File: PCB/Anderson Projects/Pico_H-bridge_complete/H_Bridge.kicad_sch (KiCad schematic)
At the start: 36 parts, among them Q1 AO3400A, Q2 AO3400A, Q3 DMP3130LQ-7, Q4 DMP3130LQ-7, Q5 MMBT3904, Q6 MMBT3904, U10 SN74LVC1G14DBV, U12 SN74LVC1G32, U13 SN74LVC1G32, U2 74LVC1G08GV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

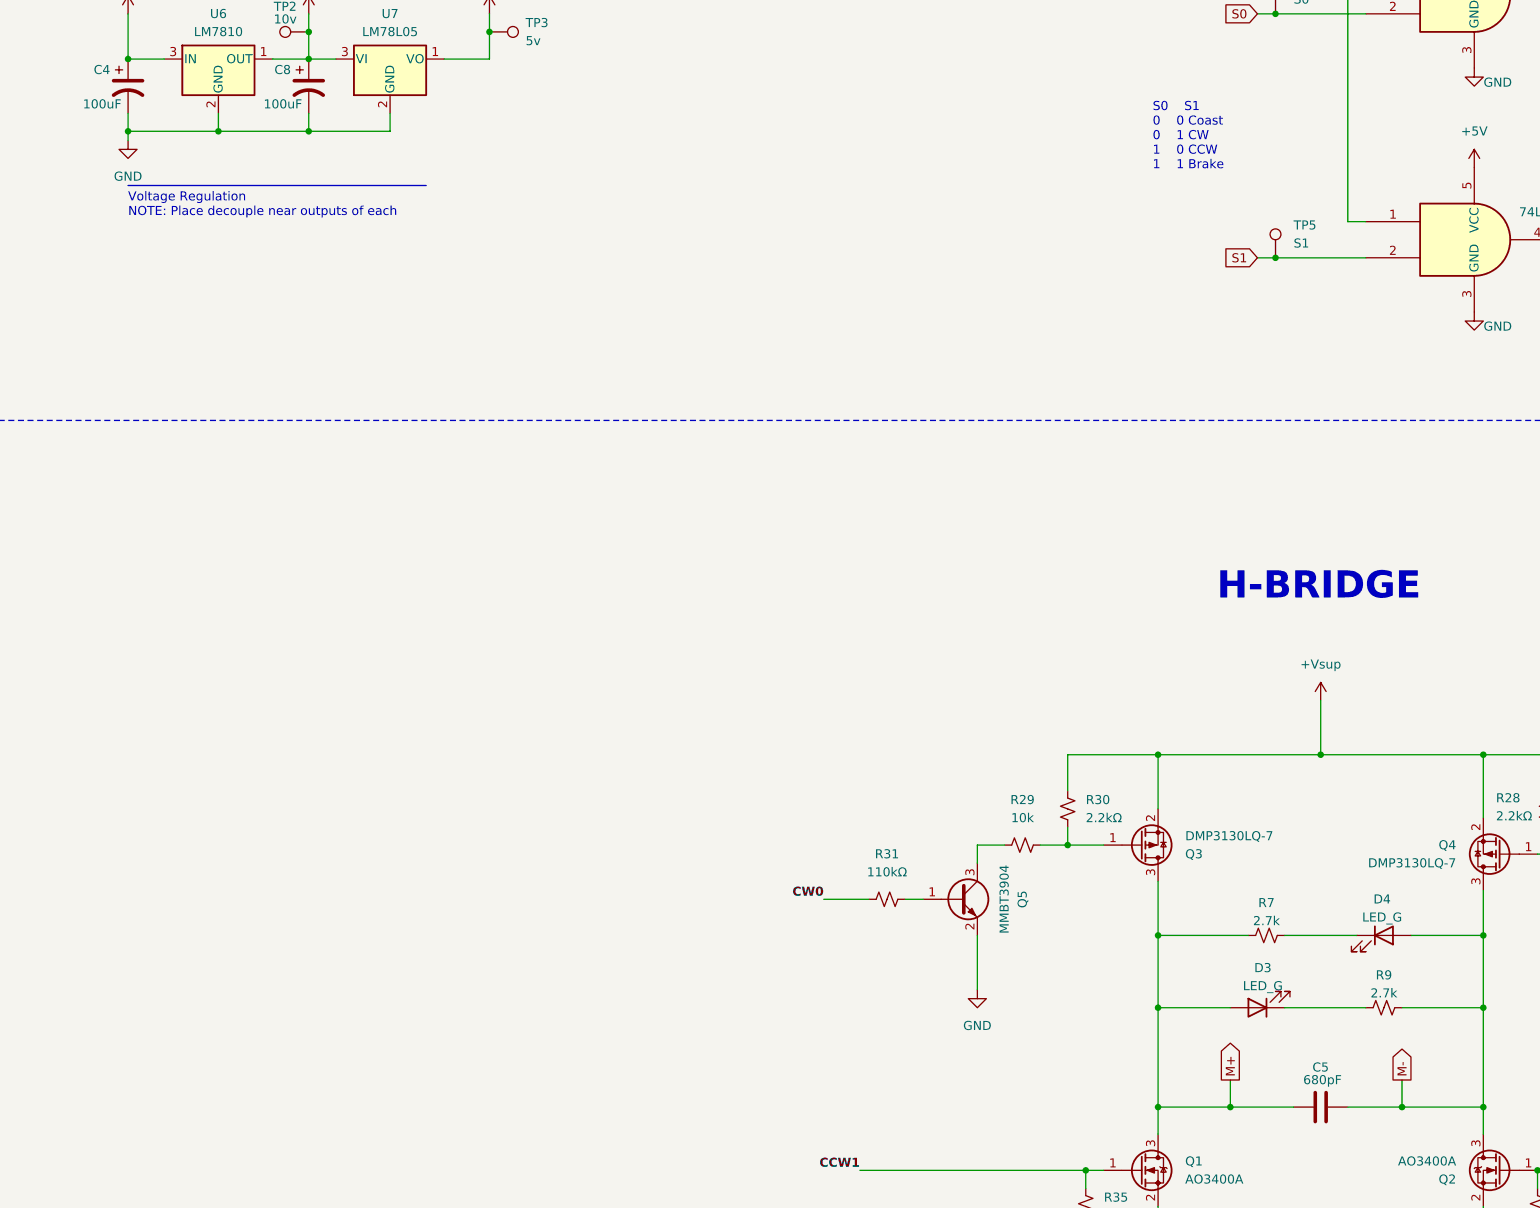
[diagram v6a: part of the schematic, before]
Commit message: Final Board version prior to testing motor with pulleys. This version would not turn the motor when connected to a generator. The Vgs values for Mosfets needed increased to 10v. Other improvements to make include removing braking functionality to simplify control to Fwd/Rev vice S0/S1.
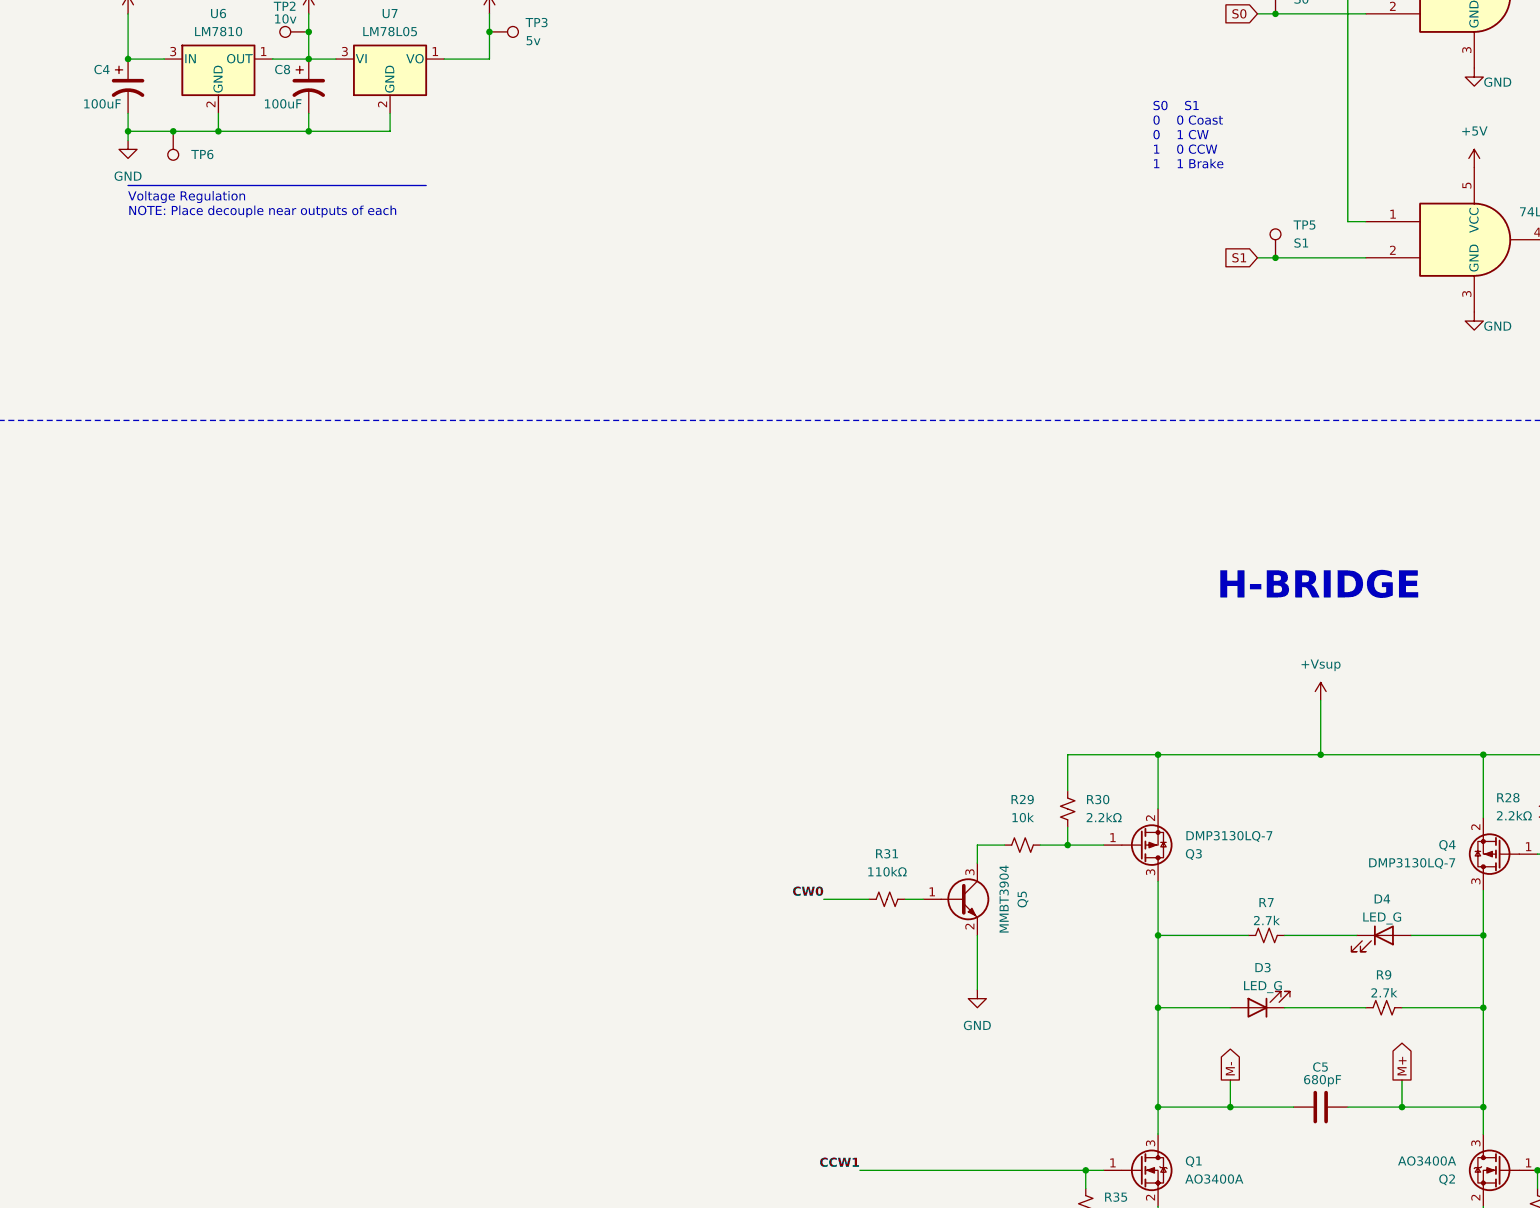
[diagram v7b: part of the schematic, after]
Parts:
- added TP6: GND, TestPoint:TestPoint_Loop_D2.60mm_Drill1.4mm_Beaded, symbol Connector:TestPoint
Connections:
- net GND: now also TP6.1
- net M+: now also C5.2, D4.2 (A), Q2.3 (D), Q4.3 (D), R9.1; no longer C5.1, D3.2 (A), Q1.3 (D), Q3.3 (D), R7.2
- net M-: now also C5.1, D3.2 (A), Q1.3 (D), Q3.3 (D), R7.2; no longer C5.2, D4.2 (A), Q2.3 (D), Q4.3 (D), R9.1
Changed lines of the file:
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@@
 	)
 	(junction
+		(at 50.8 87.63)
+		(diameter 0)
+		(color 0 0 0 0)
+	)
+	(junction
 		(at 176.53 187.96)
 		(diameter 0)
@@
 	(wire
 		(pts
+			(xy 50.8 87.63) (xy 57.15 87.63)
+		)
+		(stroke
+			(width 0)
+			(type default)
+		)
+	)
+	(wire
+		(pts
 			(xy 260.35 111.76) (xy 288.29 111.76)
 		)
@@
 	(wire
 		(pts
-			(xy 44.45 87.63) (xy 57.15 87.63)
+			(xy 44.45 87.63) (xy 50.8 87.63)
 		)
 		(stroke
@@
 	(global_label "M+"
 		(shape output)
-		(at 199.39 220.98 90)
+		(at 223.52 220.98 90)
 		(fields_autoplaced yes)
 		(effects
@@
 		)
 		(property "Intersheetrefs" "${INTERSHEET_REFS}"
-			(at 199.39 214.971 90)
+			(at 223.52 214.971 90)
 			(effects
 				(font
@@
 	(global_label "M-"
 		(shape output)
-		(at 223.52 220.98 90)
+		(at 199.39 220.98 90)
 		(fields_autoplaced yes)
 		(effects
@@
 		)
 		(property "Intersheetrefs" "${INTERSHEET_REFS}"
-			(at 223.52 214.971 90)
+			(at 199.39 214.971 90)
 			(effects
 				(font
@@
 			)
 		)
-		(property "Description" "Resistor, small US symbol"
+		(property "Description" "100mW 10k 0603"
 			(at 170.18 187.96 0)
 			(effects
@@
 			)
 		)
-		(property "Description" "Resistor, small US symbol"
+		(property "Description" "100mW 110k 0603"
 			(at 274.32 196.85 0)
 			(effects
@@
 			)
 		)
-		(property "Description" "Resistor, small US symbol"
+		(property "Description" "100mW 10k 0603"
 			(at 179.07 238.76 0)
 			(effects
@@
 			)
 		)
-		(property "Description" "Resistor, small US symbol"
+		(property "Description" "100mW 110k 0603"
 			(at 151.13 195.58 0)
 			(effects
@@
 			)
 		)
-		(property "Description" "Resistor, small US symbol"
+		(property "Description" "100mW 2.7k 0603"
 			(at 220.98 210.82 0)
 			(effects
@@
 			)
 		)
-		(property "Description" "Resistor, small US symbol"
+		(property "Description" "100mW 2.7k 0603"
 			(at 204.47 200.66 0)
 			(effects
@@
 			)
 		)
-		(property "Description" "Resistor, small US symbol"
+		(property "Description" "100mW 2.2k 0603"
 			(at 243.84 182.88 0)
 			(effects
@@
 			)
 		)
-		(property "Description" "Resistor, small US symbol"
+		(property "Description" "100mW 10k 0603"
 			(at 255.27 189.23 0)
 			(effects
@@
 			)
 		)
-		(property "Description" "Resistor, small US symbol"
+		(property "Description" "100mW 10k 0603"
 			(at 242.57 238.76 0)
 			(effects
@@
 			)
 		)
-		(property "Description" "Resistor, small US symbol"
+		(property "Description" "100mW 2.2k 0603"
 			(at 176.53 182.88 0)
 			(effects
@@
 					(unit 1)
 				)
+			)
+		)
+	)
+	(symbol
+		(lib_id "Connector:TestPoint")
+		(at 50.8 87.63 180)
+		(unit 1)
+		(exclude_from_sim no)
+		(in_bom yes)
+		(on_board yes)
+		(dnp no)
+		(fields_autoplaced yes)
+		(property "Reference" "TP6"
+			(at 53.34 90.9319 0)
+			(effects
+				(font
+					(size 1.27 1.27)
+				)
+				(justify right)
+			)
+		)
+		(property "Value" "GND"
+			(at 53.34 92.2019 0)
+			(effects
+				(font
+					(size 1.27 1.27)
+				)
+				(justify right)
+				(hide yes)
+			)
+		)
+		(property "Footprint" "TestPoint:TestPoint_Loop_D2.60mm_Drill1.4mm_Beaded"
+			(at 45.72 87.63 0)
+			(effects
+				(font
+					(size 1.27 1.27)
+				)
+				(hide yes)
+			)
+		)
+		(property "Datasheet" "~"
+			(at 45.72 87.63 0)
+			(effects
+				(font
+					(size 1.27 1.27)
+				)
+				(hide yes)
+			)
+		)
+		(property "Description" "test point"
+			(at 50.8 87.63 0)
+			(effects
+				(font
+					(size 1.27 1.27)
+				)
+				(hide yes)
+			)
+		)
+		(pin "1"
+		)
+		(instances
+			(project "Pico_H-bridge_complete"
+				(path "/6bcc676d-adc4-400e-9d1b-3d3d9a13d83a/3b9dafbc-4fc0-4ad7-a8cb-3bdf4483a920"
+					(reference "TP6")
+					(unit 1)
+				)

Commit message: (R's still mostly 0603)H-bridge circuit updated to achieve 10v Vgs. Replaced S0/S1 logic with Fwd/Rev simplified logic. Added header footprint for testing alternative capacitors. Minimized test points.
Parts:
- removed R37: 10k, Resistor_SMD:R_0603_1608Metric, symbol Device:R_Small_US
- removed TP4: S0, TestPoint:TestPoint_Plated_Hole_D2.0mm, symbol Connector:TestPoint
- removed TP5: S1, TestPoint:TestPoint_Plated_Hole_D2.0mm, symbol Connector:TestPoint
- removed U12, U13: SN74LVC1G32, Package_TO_SOT_SMD:SOT-23-5, symbol CustomBPA:SN74LVC1G32
- removed U2, U3, U4: 74LVC1G08GV, Package_TO_SOT_SMD:SOT-23-5, symbol CustomBPA:74LVC1G08GV
- added J4: 2.54 header, Connector_PinHeader_2.54mm:PinHeader_1x02_P2.54mm_Vertical, symbol Connector:Conn_01x02_Socket
- added Q7: MMBT3904, Package_TO_SOT_SMD:TO-252-2, symbol Transistor_BJT:MMBT3904
- added Q8: MMBT3904, Package_TO_SOT_SMD:SOT-23, symbol Transistor_BJT:MMBT3904
- added R22: 200Ω, Resistor_SMD:R_0603_1608Metric, symbol Device:R_Small_US
- added R23: 1kΩ, Resistor_SMD:R_0603_1608Metric, symbol Device:R_Small_US
- added R8: 22kΩ, Resistor_SMD:R_0805_2012Metric_Pad1.20x1.40mm_HandSolder, symbol Device:R_Small_US
- R26: value 10k -> 22kΩ; footprint Resistor_SMD:R_0603_1608Metric -> Resistor_SMD:R_0805_2012Metric_Pad1.20x1.40mm_HandSolder; LCSC C25804 -> C17560
- R27, R31: value 110kΩ -> 22kΩ; footprint Resistor_SMD:R_0603_1608Metric -> Resistor_SMD:R_0805_2012Metric_Pad1.20x1.40mm_HandSolder; LCSC C25805 -> C17560
- R28: value 2.2kΩ -> 10k; LCSC C4190 -> C25804
- R29: value 10k -> 200Ω; LCSC C25804 -> C17540
- R30: value 2.2kΩ -> 1kΩ; LCSC C4190 -> C17513
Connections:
- net S0 is gone; now on net CCW1: U8.2
- net S1 is gone; now on net Fwd/Rev: U9.2
- net +10V: now also R28.1, R35.1
- net CCW0: now also U8.4, R8.2; no longer R27.2
- net CCW1: now also R26.1, U10.4; no longer Q1.1 (G), R35.1
- net CW0: now also U9.4
- net GND: now also Q7.2 (E), Q8.2 (E); no longer R35.2
- net M+: now also J4.1 (Pin_1)
- net M-: now also J4.2 (Pin_2)
- net at Q6.1 (B): now also R8.1; no longer R27.1
- net Fwd/Rev: now reaches U10.2
- net Fwd/Rev: now also R27.1
- net at Q6.3 (C): now also R22.2; no longer R26.2
- net +Vsup renamed +12V
- net +12V: now also R23.2; no longer R28.1
- net CW1: no longer names the net of Q2.1 (G)
- net CW1: now also R28.2, Q8.3 (C)
- new net: Q1.1 (G), Q7.3 (C), R35.2
- new net: Q4.1 (G), R22.1, R23.1
- new net: Q8.1 (B), R27.2
- new net: Q7.1 (B), R26.2
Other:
- note removed: "S0 S1 0 0 Coast 0 1 CW 1 0 CCW 1 1 Brake"
- moved on the sheet: C4, C8, JP1, R35, TP2, TP3, TP6, U10, U6, U7, U8, U9
